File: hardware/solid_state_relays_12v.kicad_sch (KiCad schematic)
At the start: 82 parts, among them J1 1190297, J2 1190297, J3 1190297, J4 1190297, J5 1190297, J6 1190297, J7 1190297, J8 1190297, Q1 IRF4905PBF, Q2 IRF4905PBF, Q3 IRF4905PBF, Q4 IRF4905PBF, Q5 IRF4905PBF, Q6 IRF4905PBF, Q7 IRF4905PBF, Q8 IRF4905PBF

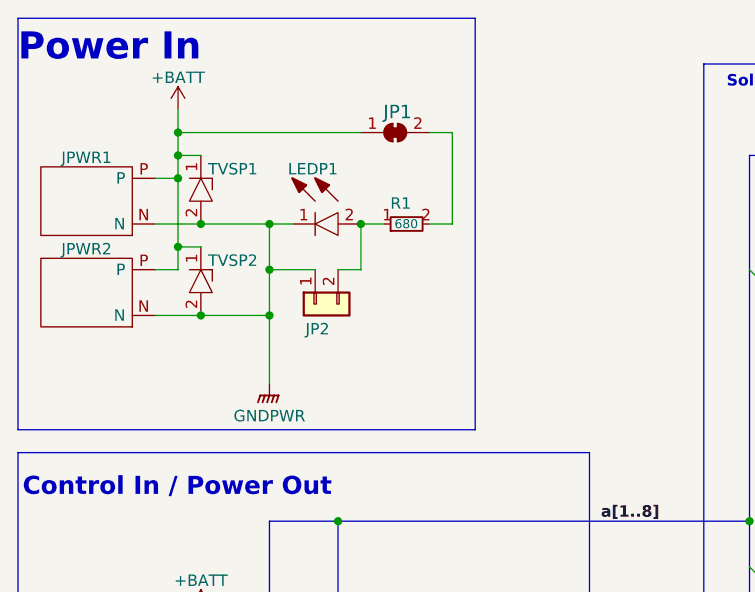
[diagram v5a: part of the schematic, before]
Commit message: Added power header pins for fans
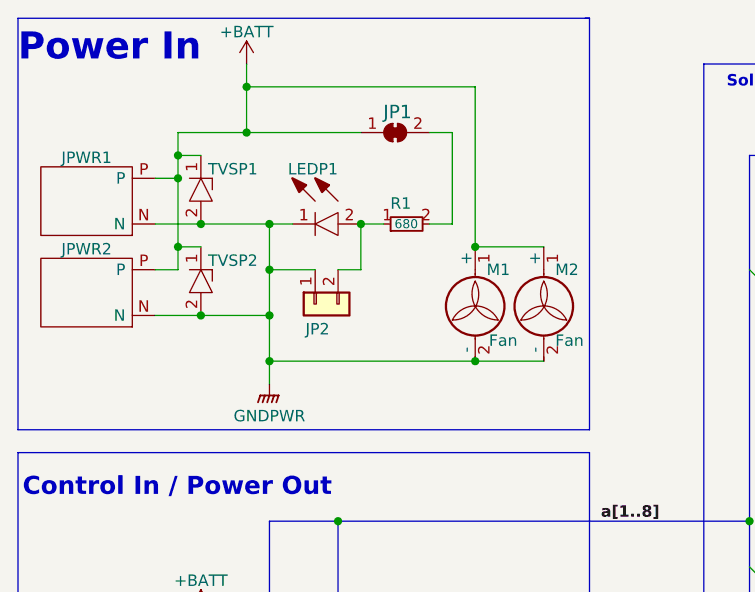
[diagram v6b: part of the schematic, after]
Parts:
- added M1, M2: Fan, Connector_PinHeader_2.54mm:PinHeader_1x02_P2.54mm_Vertical, symbol Motor:Fan
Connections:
- net +BATT: now also M1.1 (+), M2.1 (+)
- net GNDPWR: now also M1.2 (-), M2.2 (-)
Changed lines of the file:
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@@
   (title_block
     (title "Solid State Relays 12V")
-    (date "2023-01-10")
-    (rev "0.0.9")
+    (date "2023-01-21")
+    (rev "0.0.10")
     (comment 2 "creativecommons.org/licenses/by/4.0/")
     (comment 3 "License: CC By 4.0")
@@
   (junction (at 111.76 111.76) (diameter 0) (color 0 0 0 0)
   )
+  (junction (at 43.18 53.34) (diameter 0) (color 0 0 0 0)
+  )
   (junction (at 213.36 101.6) (diameter 0) (color 0 0 0 0)
   )
@@
   (junction (at 106.68 157.48) (diameter 0) (color 0 0 0 0)
   )
-  (junction (at 33.02 27.94) (diameter 0) (color 0 0 0 0)
-  )
   (junction (at 220.98 157.48) (diameter 0) (color 0 0 0 0)
   )
@@
   (junction (at 149.86 53.34) (diameter 0) (color 0 0 0 0)
   )
+  (junction (at 40.64 27.94) (diameter 0) (color 0 0 0 0)
+  )
+  (junction (at 40.64 22.86) (diameter 0) (color 0 0 0 0)
+  )
   (junction (at 27.94 139.7) (diameter 0) (color 0 0 0 0)
   )
@@
   (junction (at 33.02 40.64) (diameter 0) (color 0 0 0 0)
   )
+  (junction (at 66.04 40.64) (diameter 0) (color 0 0 0 0)
+  )
   (junction (at 218.44 101.6) (diameter 0) (color 0 0 0 0)
   )
@@
   (junction (at 35.56 38.1) (diameter 0) (color 0 0 0 0)
   )
+  (junction (at 66.04 53.34) (diameter 0) (color 0 0 0 0)
+  )
   (junction (at 50.8 71.12) (diameter 0) (color 0 0 0 0)
   )
@@
     (stroke (width 0) (type default) (color 0 0 0 0))
   )
+  (wire (pts (xy 66.04 53.34) (xy 73.66 53.34))
+    (stroke (width 0) (type default) (color 0 0 0 0))
+  )
   (wire (pts (xy 111.76 68.58) (xy 111.76 78.74))
     (stroke (width 0) (type default) (color 0 0 0 0))
@@
     (stroke (width 0) (type default) (color 0 0 0 0))
   )
+  (wire (pts (xy 66.04 22.86) (xy 66.04 40.64))
+    (stroke (width 0) (type default) (color 0 0 0 0))
+  )
   (wire (pts (xy 208.28 134.62) (xy 213.36 134.62))
     (stroke (width 0) (type default) (color 0 0 0 0))
@@
     (stroke (width 0) (type default) (color 0 0 0 0))
   )
-  (polyline (pts (xy 15.24 15.24) (xy 66.04 15.24))
+  (polyline (pts (xy 15.24 15.24) (xy 78.74 15.24))
     (stroke (width 0) (type default) (color 0 0 0 0))
   )
@@
     (stroke (width 0) (type default) (color 0 0 0 0))
   )
+  (wire (pts (xy 40.64 20.32) (xy 40.64 22.86))
+    (stroke (width 0) (type default) (color 0 0 0 0))
+  )
   (wire (pts (xy 21.59 91.44) (xy 21.59 93.98))
     (stroke (width 0) (type default) (color 0 0 0 0))
@@
     (stroke (width 0) (type default) (color 0 0 0 0))
   )
-  (wire (pts (xy 33.02 27.94) (xy 53.34 27.94))
+  (wire (pts (xy 33.02 27.94) (xy 40.64 27.94))
     (stroke (width 0) (type default) (color 0 0 0 0))
   )
@@
     (stroke (width 0) (type default) (color 0 0 0 0))
   )
+  (wire (pts (xy 66.04 40.64) (xy 73.66 40.64))
+    (stroke (width 0) (type default) (color 0 0 0 0))
+  )
   (wire (pts (xy 220.98 124.46) (xy 218.44 124.46))
     (stroke (width 0) (type default) (color 0 0 0 0))
@@
     (stroke (width 0) (type default) (color 0 0 0 0))
   )
-  (wire (pts (xy 33.02 25.4) (xy 33.02 27.94))
-    (stroke (width 0) (type default) (color 0 0 0 0))
-  )
-  (polyline (pts (xy 66.04 15.24) (xy 66.04 60.96))
+  (wire (pts (xy 40.64 27.94) (xy 53.34 27.94))
     (stroke (width 0) (type default) (color 0 0 0 0))
   )
@@
     (stroke (width 0) (type default) (color 0 0 0 0))
   )
-  (wire (pts (xy 43.18 48.26) (xy 43.18 55.88))
-    (stroke (width 0) (type default) (color 0 0 0 0))
-  )
   (wire (pts (xy 109.22 86.36) (xy 106.68 86.36))
     (stroke (width 0) (type default) (color 0 0 0 0))
@@
     (stroke (width 0) (type default) (color 0 0 0 0))
   )
-  (polyline (pts (xy 66.04 60.96) (xy 15.24 60.96))
+  (polyline (pts (xy 78.74 60.96) (xy 15.24 60.96))
     (stroke (width 0) (type default) (color 0 0 0 0))
   )
@@
     (stroke (width 0) (type default) (color 0 0 0 0))
   )
+  (wire (pts (xy 43.18 48.26) (xy 43.18 53.34))
+    (stroke (width 0) (type default) (color 0 0 0 0))
+  )
   (wire (pts (xy 152.4 101.6) (xy 152.4 134.62))
     (stroke (width 0) (type default) (color 0 0 0 0))
@@
     (stroke (width 0) (type default) (color 0 0 0 0))
   )
+  (polyline (pts (xy 78.74 15.24) (xy 78.74 60.96))
+    (stroke (width 0) (type default) (color 0 0 0 0))
+  )
   (wire (pts (xy 220.98 116.84) (xy 220.98 119.38))
     (stroke (width 0) (type default) (color 0 0 0 0))
@@
     (stroke (width 0) (type default) (color 0 0 0 0))
   )
+  (wire (pts (xy 43.18 53.34) (xy 66.04 53.34))
+    (stroke (width 0) (type default) (color 0 0 0 0))
+  )
   (wire (pts (xy 213.36 101.6) (xy 213.36 106.68))
     (stroke (width 0) (type default) (color 0 0 0 0))
@@
     (stroke (width 0) (type default) (color 0 0 0 0))
   )
+  (wire (pts (xy 40.64 22.86) (xy 40.64 27.94))
+    (stroke (width 0) (type default) (color 0 0 0 0))
+  )
   (wire (pts (xy 106.68 119.38) (xy 106.68 124.46))
     (stroke (width 0) (type default) (color 0 0 0 0))
@@
     (stroke (width 0) (type default) (color 0 0 0 0))
   )
+  (wire (pts (xy 40.64 22.86) (xy 66.04 22.86))
+    (stroke (width 0) (type default) (color 0 0 0 0))
+  )
   (wire (pts (xy 53.34 96.52) (xy 58.42 96.52))
     (stroke (width 0) (type default) (color 0 0 0 0))
@@
     (stroke (width 0) (type default) (color 0 0 0 0))
   )
+  (polyline (pts (xy 78.232 15.24) (xy 78.74 15.24))
+    (stroke (width 0) (type default) (color 0 0 0 0))
+  )
+  (wire (pts (xy 43.18 53.34) (xy 43.18 55.88))
+    (stroke (width 0) (type default) (color 0 0 0 0))
+  )
   (polyline (pts (xy 43.18 160.02) (xy 43.18 182.88))
     (stroke (width 0) (type default) (color 0 0 0 0))
@@
     (pin "2")
   )
+  (symbol (lib_id "Motor:Fan") (at 73.66 48.26 0) (unit 1)
+    (in_bom yes) (on_board yes)
+    (property "Reference" "M2" (id 0) (at 74.93 43.18 0)
+      (effects (font (size 1.27 1.27)) (justify left))
+    )
+    (property "Value" "Fan" (id 1) (at 74.93 51.054 0)
+      (effects (font (size 1.27 1.27)) (justify left))
+    )
+    (property "Footprint" "Connector_PinHeader_2.54mm:PinHeader_1x02_P2.54mm_Vertical" (id 2) (at 73.66 48.006 0)
+      (effects (font (size 1.27 1.27)) hide)
+    )
+    (property "Datasheet" "~" (id 3) (at 73.66 48.006 0)
+      (effects (font (size 1.27 1.27)) hide)
+    )
+    (pin "1")
+    (pin "2")
+  )
   (symbol (lib_id "dragon_mobile:SM6T33AY") (at 35.56 30.48 270) (unit 1)
     (in_bom yes) (on_board yes)
@@
     (pin "1")
   )
-  (symbol (lib_id "power:+BATT") (at 33.02 25.4 0) (unit 1)
+  (symbol (lib_id "power:+BATT") (at 40.64 20.32 0) (unit 1)
     (in_bom yes) (on_board yes)
-    (property "Reference" "#PWR02" (id 0) (at 33.02 29.21 0)
+    (property "Reference" "#PWR02" (id 0) (at 40.64 24.13 0)
       (effects (font (size 1.27 1.27)) hide)
     )
-    (property "Value" "+BATT" (id 1) (at 33.02 21.844 0))
-    (property "Footprint" "" (id 2) (at 33.02 25.4 0)
+    (property "Value" "+BATT" (id 1) (at 40.64 16.764 0))
+    (property "Footprint" "" (id 2) (at 40.64 20.32 0)
       (effects (font (size 1.27 1.27)) hide)
     )
-    (property "Datasheet" "" (id 3) (at 33.02 25.4 0)
+    (property "Datasheet" "" (id 3) (at 40.64 20.32 0)
       (effects (font (size 1.27 1.27)) hide)
     )
@@
     )
   )
+  (symbol (lib_id "Motor:Fan") (at 66.04 48.26 0) (unit 1)
+    (in_bom yes) (on_board yes)
+    (property "Reference" "M1" (id 0) (at 67.31 43.18 0)
+      (effects (font (size 1.27 1.27)) (justify left))
+    )
+    (property "Value" "Fan" (id 1) (at 67.564 51.054 0)
+      (effects (font (size 1.27 1.27)) (justify left))
+    )
+    (property "Footprint" "Connector_PinHeader_2.54mm:PinHeader_1x02_P2.54mm_Vertical" (id 2) (at 66.04 48.006 0)
+      (effects (font (size 1.27 1.27)) hide)
+    )
+    (property "Datasheet" "~" (id 3) (at 66.04 48.006 0)
+      (effects (font (size 1.27 1.27)) hide)
+    )
+    (pin "1")
+    (pin "2")
+  )
   (symbol (lib_id "Device:R_Small") (at 205.74 101.6 90) (unit 1)
     (in_bom yes) (on_board yes)
@@
       (reference "LEDP1") (unit 1) (value "LTST-C190KGKT") (footprint "dragon_mobile:LEDC1608X80N")
     )
+    (path "/d545b974-18fe-46f3-a4d7-55be7cb5dc36"
+      (reference "M1") (unit 1) (value "Fan") (footprint "Connector_PinHeader_2.54mm:PinHeader_1x02_P2.54mm_Vertical")
+    )
+    (path "/5a192482-0668-476b-8ae3-93d4cd301205"
+      (reference "M2") (unit 1) (value "Fan") (footprint "Connector_PinHeader_2.54mm:PinHeader_1x02_P2.54mm_Vertical")
+    )
     (path "/38325c2d-023b-4f86-8f11-709b659b391c"

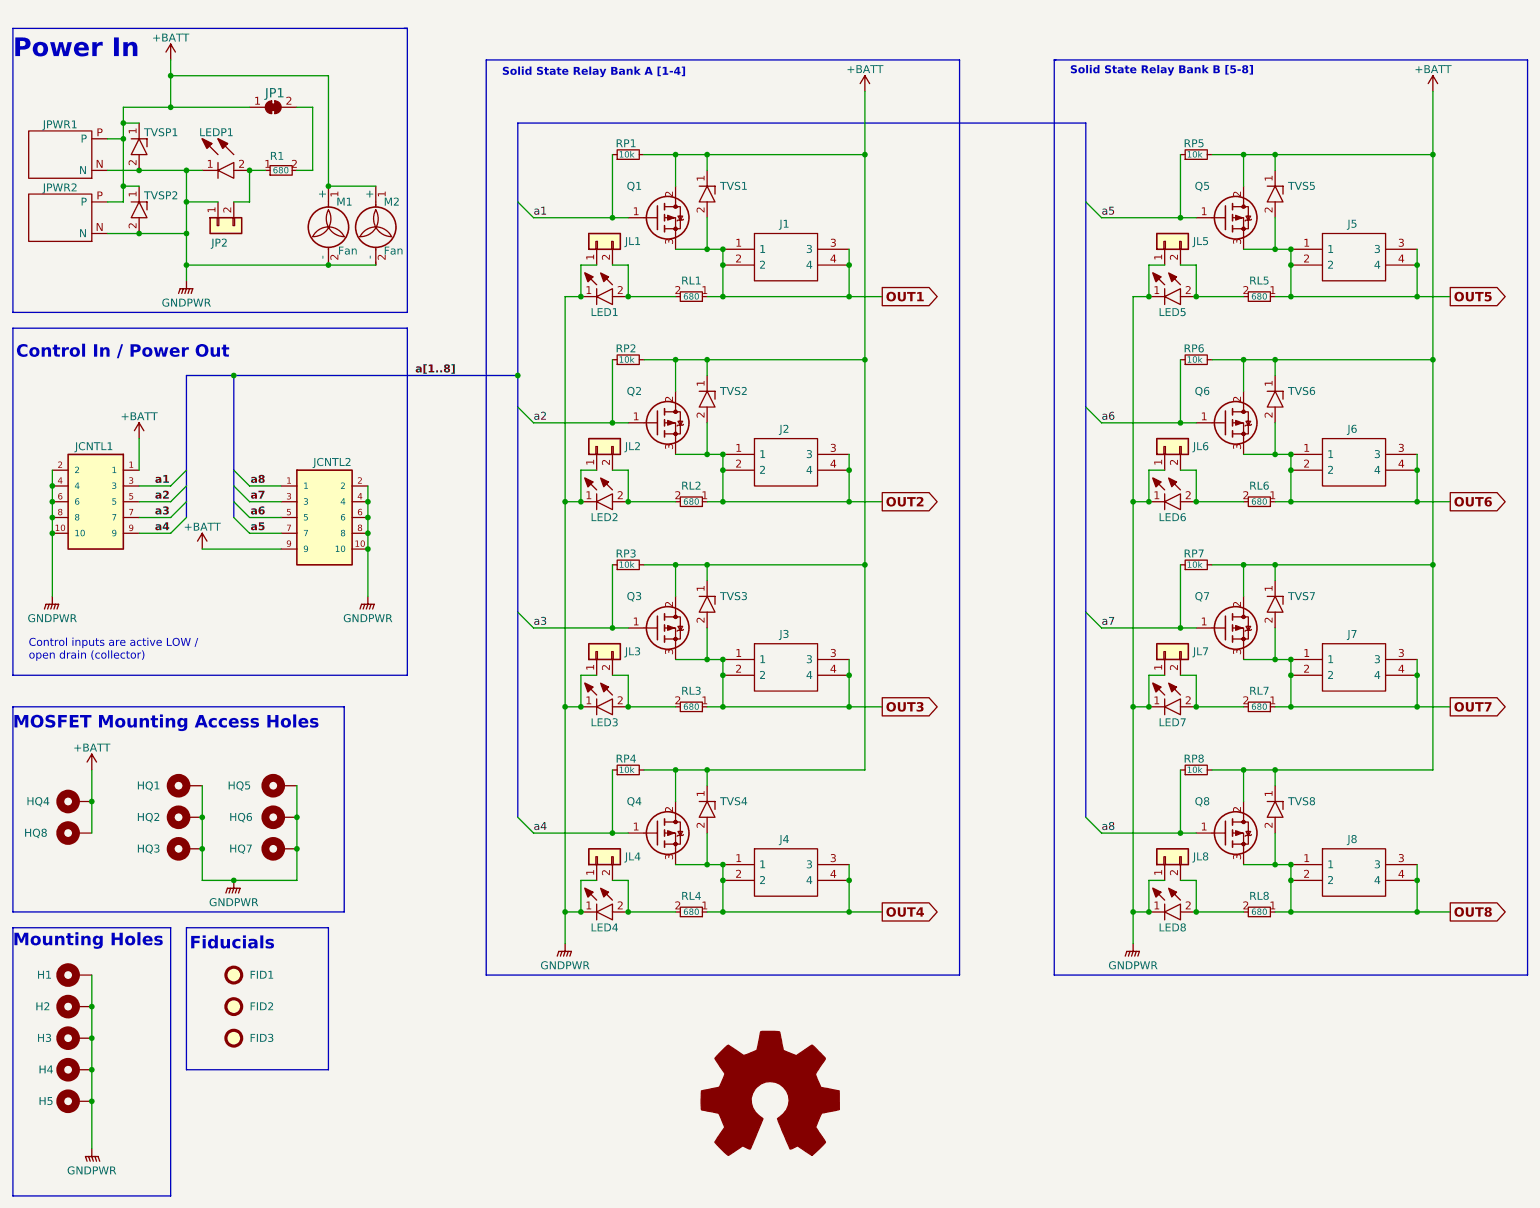
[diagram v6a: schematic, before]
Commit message: Changed schematic to hierarchical style with mutliple sheets
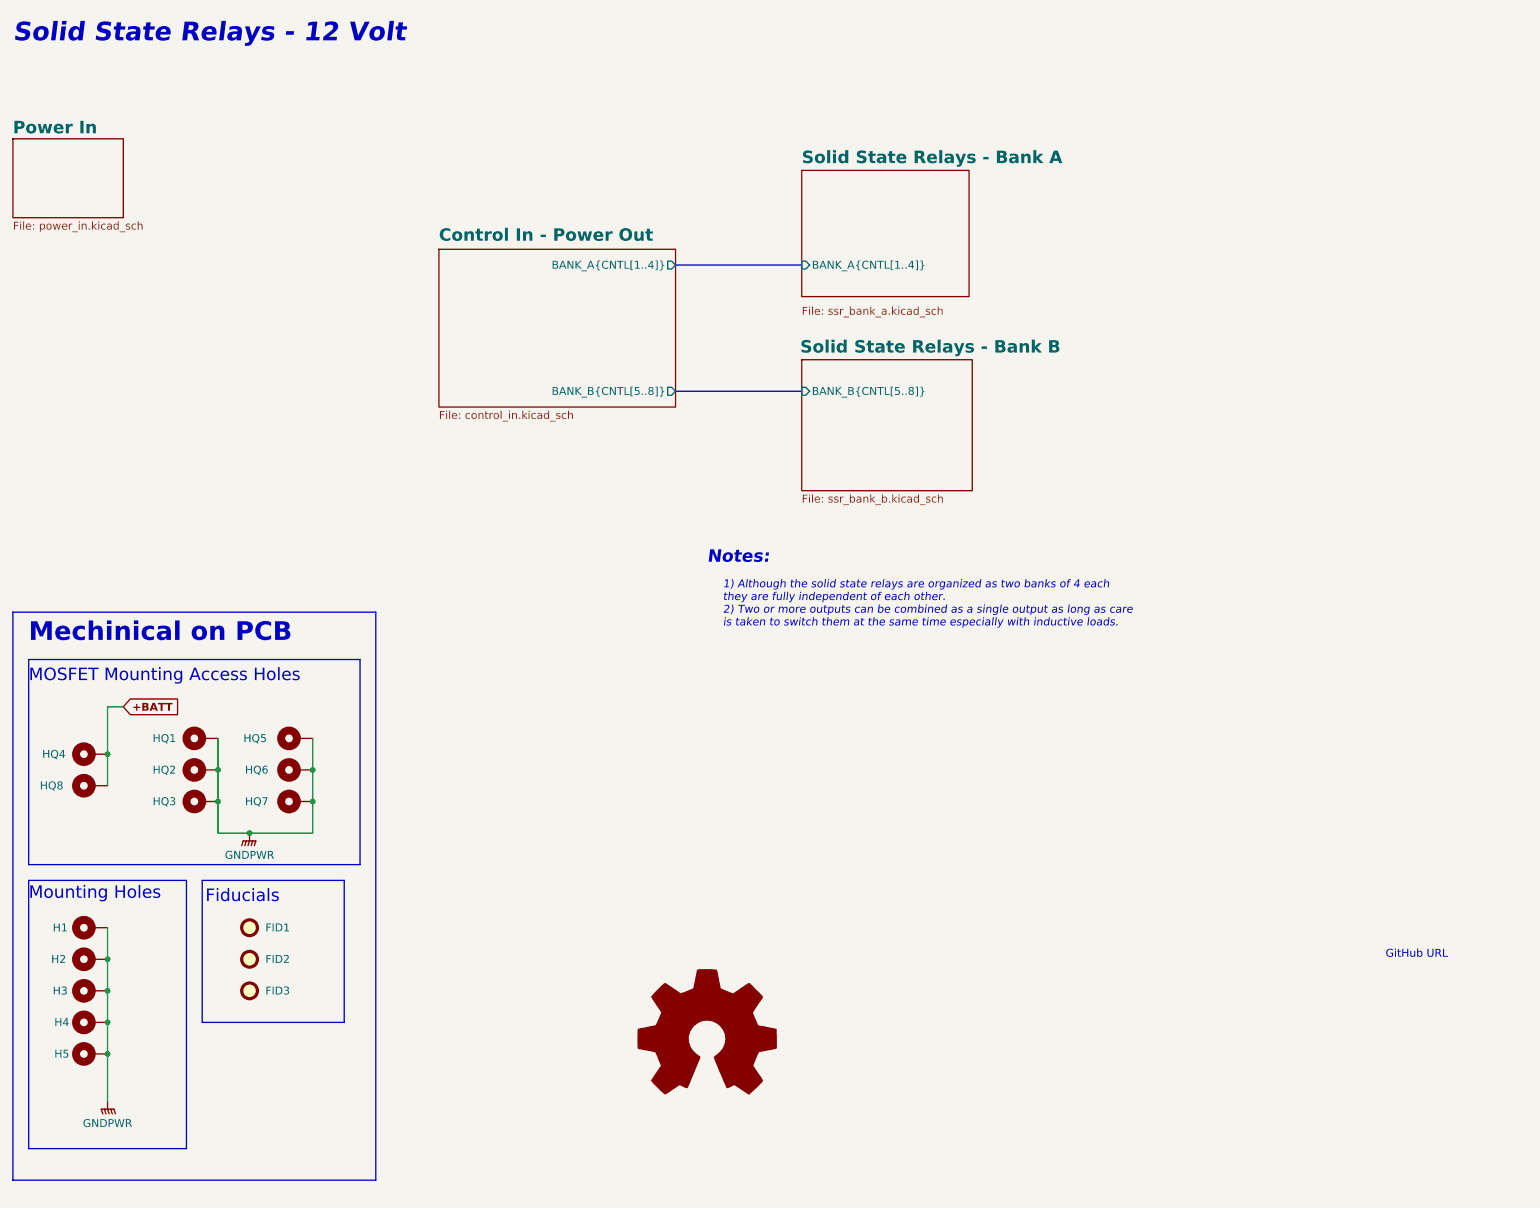
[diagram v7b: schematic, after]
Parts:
- removed J1, J2, J3, J4, J5, J6, J7, J8: 1190297, dragon_mobile:1190297, symbol dragon_mobile:1190297
- removed JCNTL1, JCNTL2: SHF-105-01-L-D-RA, dragon_mobile:SAMTEC_SHF-105-01-L-D-RA, symbol Connector_Samtec:SHF-105-01-L-D-RA
- removed JL1, JL2, JL3, JL4, JL5, JL6, JL7, JL8, JP2: Conn_01x02, dragon_mobile:PinHeader_1x02_P1.00mm_Vertical, symbol dragon_mobile:Conn_01x02
- removed JP1: SolderJumper_2_Bridged, Jumper:SolderJumper-2_P1.3mm_Bridged_RoundedPad1.0x1.5mm, symbol Jumper:SolderJumper_2_Bridged
- removed JPWR1, JPWR2: XT60PW-M, dragon_mobile:XT60PWM, symbol dragon_mobile:XT60PW-M
- removed LED1, LED2, LED3, LED4, LED5, LED6, LED7, LED8: LTST-C190KFKT, dragon_mobile:LEDC1607X80N, symbol dragon_mobile:LTST-C190KFKT
- removed LEDP1: LTST-C190KGKT, dragon_mobile:LEDC1608X80N, symbol dragon_mobile:LTST-C190KGKT
- removed M1, M2: Fan, Connector_PinHeader_2.54mm:PinHeader_1x02_P2.54mm_Vertical, symbol Motor:Fan
- removed Q1, Q2, Q3, Q4, Q5, Q6, Q7, Q8: IRF4905PBF, dragon_mobile:TO254P469X1042X1967-3P, symbol dragon_mobile:IRF4905PBF
- removed R1, RL1, RL2, RL3, RL4, RL5, RL6, RL7, RL8: 680, dragon_mobile:RESC2012X65N, symbol dragon_mobile:SDR10EZPJ152
- removed RP1, RP2, RP3, RP4, RP5, RP6, RP7, RP8: 10k, dragon_mobile:RESC2012X65N, symbol Device:R_Small
- removed TVS1, TVS2, TVS3, TVS4, TVS5, TVS6, TVS7, TVS8: SM6T16V5AY, dragon_mobile:SMBJ36CATR, symbol dragon_mobile:SM6T30AY
- removed TVSP1, TVSP2: SM6T16V5AY, dragon_mobile:SMBJ36CATR, symbol dragon_mobile:SM6T33AY
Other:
- added sheet Control In - Power Out (control_in.kicad_sch)
- added sheet Power In (power_in.kicad_sch)
- added sheet Solid State Relays - Bank A (ssr_bank_a.kicad_sch)
- added sheet Solid State Relays - Bank B (ssr_bank_b.kicad_sch)
- note added: "1) Although the solid state relays are organized as two banks of 4 each they are fully independent of each other. 2) Two or more outputs can be combined as a single output as long as care is taken to switch them at the same time especially with inductive loads."
- note added: "GitHub URL"
- note added: "Mechinical on PCB"
- note added: "Notes:"
- note added: "Solid State Relays - 12 Volt"
- note removed: "Control In / Power Out"
- note removed: "Control inputs are active LOW / open drain (collector)"
- note removed: "Power In"
- note removed: "Solid State Relay Bank A [1-4]"
- note removed: "Solid State Relay Bank B [5-8]"
- moved on the sheet: FID1, FID2, FID3, H1, H2, H3, H4, H5, HQ1, HQ2, HQ3, HQ4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

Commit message: Via spamming #1
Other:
- sheet Control In - Power Out ports: added +BATT; removed none
- sheet Power In ports: added +BATT; removed none
- sheet Solid State Relays - Bank A ports: added +BATT; removed none
- sheet Solid State Relays - Bank B ports: added +BATT; removed none
